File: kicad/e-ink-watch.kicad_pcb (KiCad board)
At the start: 4 copper layers, 40 x 40 mm, 42 parts, among them SW1 BTN1, SW2 BTN2, SW3 BTN3, U1 MDBT50Q-1MV2, U2 BQ25120A

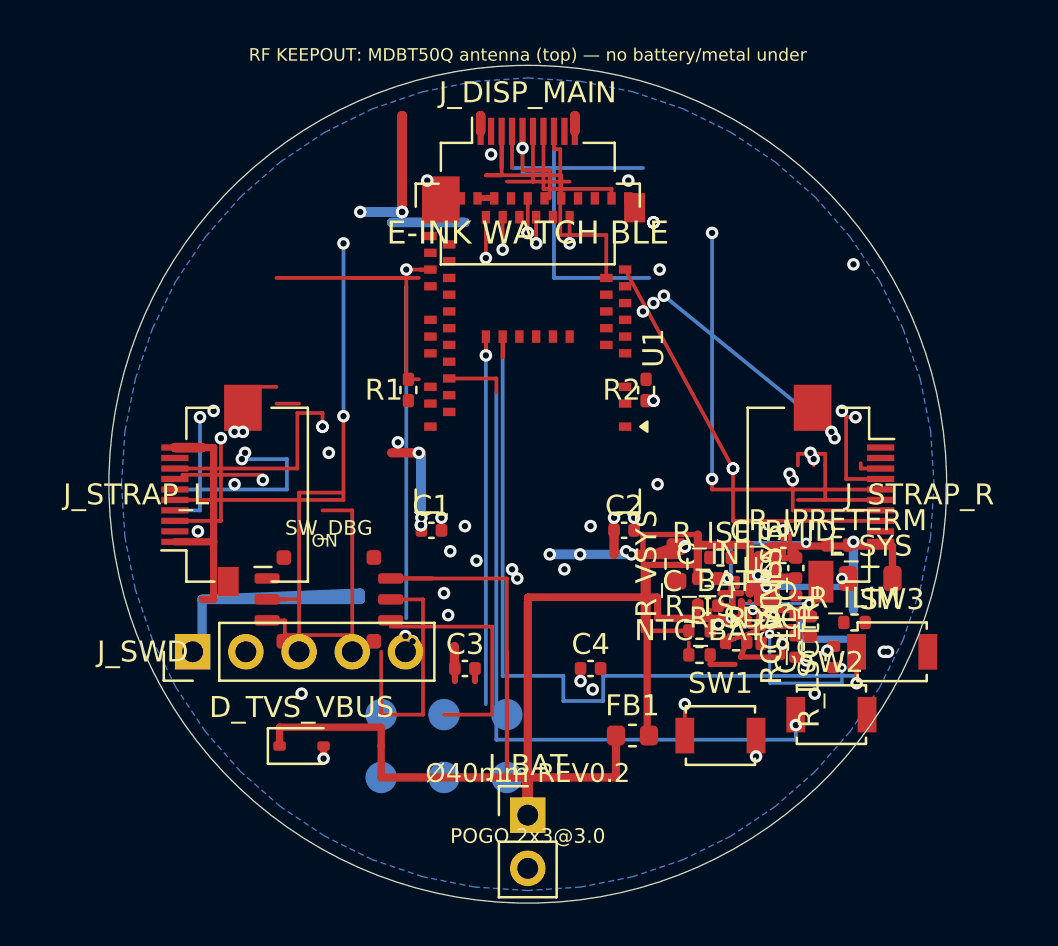
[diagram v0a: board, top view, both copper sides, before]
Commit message: PCB Pass-P..AE: shorting 0, unconnected 84→12
Clear DRC shorts then cut open nets with placement moves.
C_PMID stitched; ISET/VSYS/TS landed; SWD/SPI mostly closed.
Keep power-priority and PMID↔VBUS at 0. Do not apply VBUS on dock.
Session log and DRC reports under kicad/reports/; drop churn _drc_* temps.
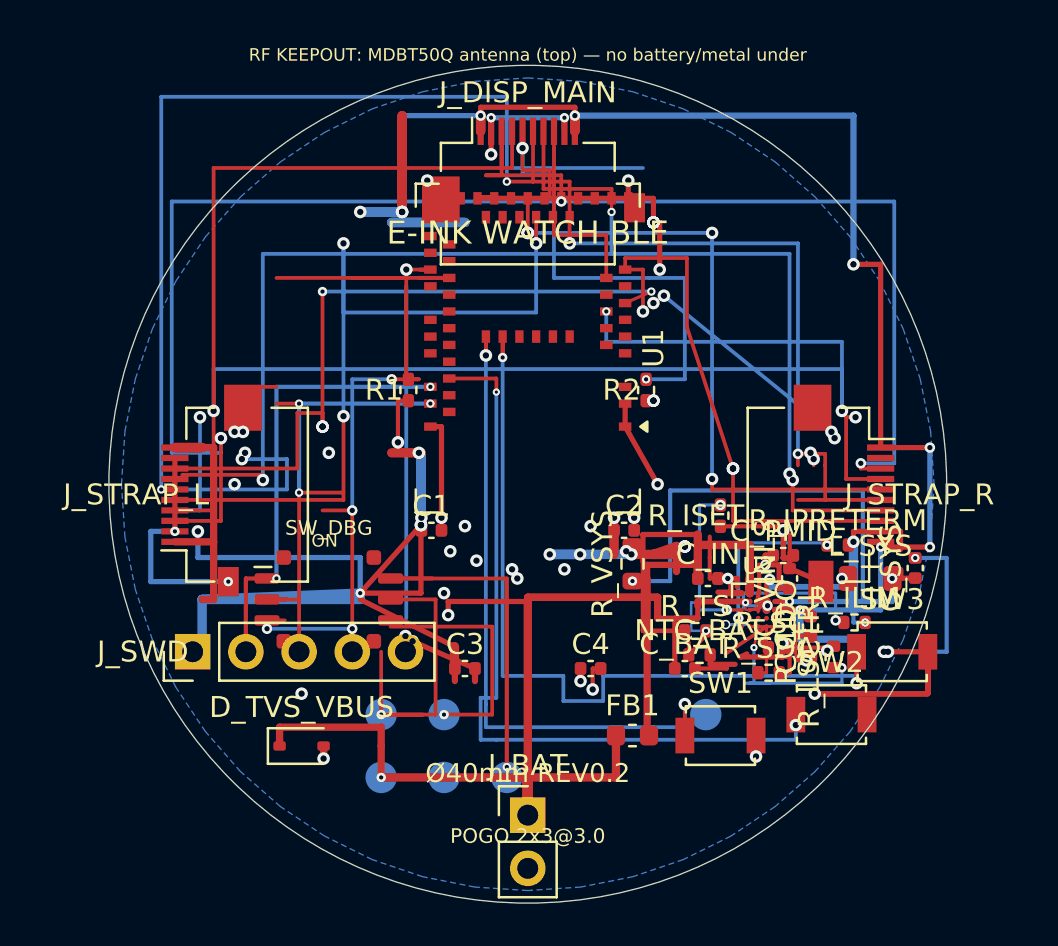
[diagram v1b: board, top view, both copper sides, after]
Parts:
- moved TP6 9.50 mm to (108.5, 111.0)
- moved C_SYS 5.70 mm to (118.5, 104.0)
- moved C_BAT 3.20 mm to (107.5, 108.8)
- moved R_SDA 2.12 mm to (111.5, 109.0)
- moved R_VSYS 2.10 mm to (105.0, 103.8)
- moved R_ISET 2.00 mm to (109.2, 101.5), turned to 90 degrees
- moved C_VINLS 1.33 mm to (112.5, 104.5)
- moved R_CD 0.70 mm to (113.5, 107.8)
- moved R_SCL 0.40 mm to (112.0, 107.8)
- moved R_TS 0.20 mm to (108.0, 107.0)
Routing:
- net GND: track 38.1 -> 120.3 mm, vias 35 -> 42
- net EPD_SCK: track 7.35 -> 89.2 mm, vias 3 -> 4
- net EPD_MOSI: track 16.6 -> 80.4 mm, vias 1 -> 4
- net EPD_DC: track 15.5 -> 78.6 mm, vias 3 -> 6
- net 3V3_DISP: track 46.7 -> 103.6 mm, vias 6 -> 13
- net EPD_RST: track 16.3 -> 65.2 mm, vias 3 -> 4
- net 3V3: track 53.0 -> 99.7 mm, vias 23 -> 25
- net EPD_BUSY_L: track 10.4 -> 33.9 mm, vias 2 -> 4
- net SWDIO: track 0.45 -> 21.5 mm, vias 0 -> 2
- net VSYS: track 12.6 -> 29.2 mm, vias 0 -> 3
- net EPD_CS_L: track 21.5 -> 37.3 mm
- net nRESET: track 27.8 -> 40.3 mm, vias 0 -> 4
- net BTN1: track 19.9 -> 31.6 mm
- net SWDCLK: track 13.3 -> 23.8 mm, vias 0 -> 3
- net EPD_CS_R: track 22.0 -> 30.8 mm
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
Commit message: PCB Pass-AF: unique switch UUIDs, close SW2 and strap-R GND.
Unconnected 12→10 with shorting_items held at 0 (KiCad 9.0.9 DRC).
Copied SW1/SW2/SW3 pads shared UUIDs, so DRC mislabeled SW2 as SW3.
J_STRAP_R pad 2 now exits on the cable side to avoid FH12 neighbors.

Co-authored-by: illiapliukhin <illiapliukhin@users.noreply.github.com>
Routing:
- net GND: track 120.3 -> 139.0 mm, vias 42 -> 43
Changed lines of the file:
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@@
 		(net 2)
+	)
+	(segment
+		(start 117.2 108.0)
+		(end 117.2 111.0)
+		(width 0.2)
+		(layer "B.Cu")
+		(net 1)
+	)
+	(segment
+		(start 117.2 111.0)
+		(end 113.7 111.0)
+		(width 0.2)
+		(layer "B.Cu")
+		(net 1)
+	)
+	(segment
+		(start 113.7 111.0)
+		(end 113.7 110.0)
+		(width 0.2)
+		(layer "B.Cu")
+		(net 1)
+	)
+	(segment
+		(start 116.2 111.0)
+		(end 113.7 110.0)
+		(width 0.25)
+		(layer "F.Cu")
+		(net 1)
+	)
+	(segment
+		(start 116.85 98.75)
+		(end 118.4 98.75)
+		(width 0.15)
+		(layer "F.Cu")
+		(net 1)
+	)
+	(via
+		(at 118.4 98.75)
+		(size 0.4)
+		(drill 0.2)
+		(layers "F.Cu" "B.Cu")
+		(net 1)
+	)
+	(segment
+		(start 118.4 98.75)
+		(end 118.4 99.9)
+		(width 0.2)
+		(layer "B.Cu")
+		(net 1)
+	)
+	(segment
+		(start 118.4 99.9)
+		(end 114.65 99.9)
+		(width 0.2)
+		(layer "B.Cu")
+		(net 1)
+	)
+	(segment
+		(start 114.65 99.9)
+		(end 114.65 97.8)
+		(width 0.2)
+		(layer "B.Cu")
+		(net 1)
 	)
 	(via

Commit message: PCB Pass-AG: slide ISET via west in-place, hold shorting 0.
Open the U2 west C-row pocket without sexpr reorder. Delete-first
edits promoted latent TS/VBAT, ILIM/PMID, and CD/SCL shorts; those
attempts are reverted. Unconnected stays at 10.

Co-authored-by: illiapliukhin <illiapliukhin@users.noreply.github.com>
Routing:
- net ISET: track 8.01 -> 8.96 mm
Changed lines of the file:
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@@
 	)
 	(via
-		(at 109.5 106.0)
-		(size 0.5)
-		(drill 0.25)
+		(at 108.55 106.0)
+		(size 0.35)
+		(drill 0.15)
 		(layers "F.Cu" "B.Cu")
 		(net 34)
 	)
 	(segment
-		(start 109.5 106.0)
+		(start 108.55 106.0)
 		(end 110.2 106.0)
 		(width 0.15)
